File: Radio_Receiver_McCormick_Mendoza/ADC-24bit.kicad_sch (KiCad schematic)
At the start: 38 parts, among them J21 SDR Out, J22 Q_OUT, J30 Q_OUT, J31 Q_OUT, J32 Q_OUT, J41 V_DIV, J42 VDDA/2, J7 I_OUT, U10 OPA1612AxD, U12 PCM1808PWR

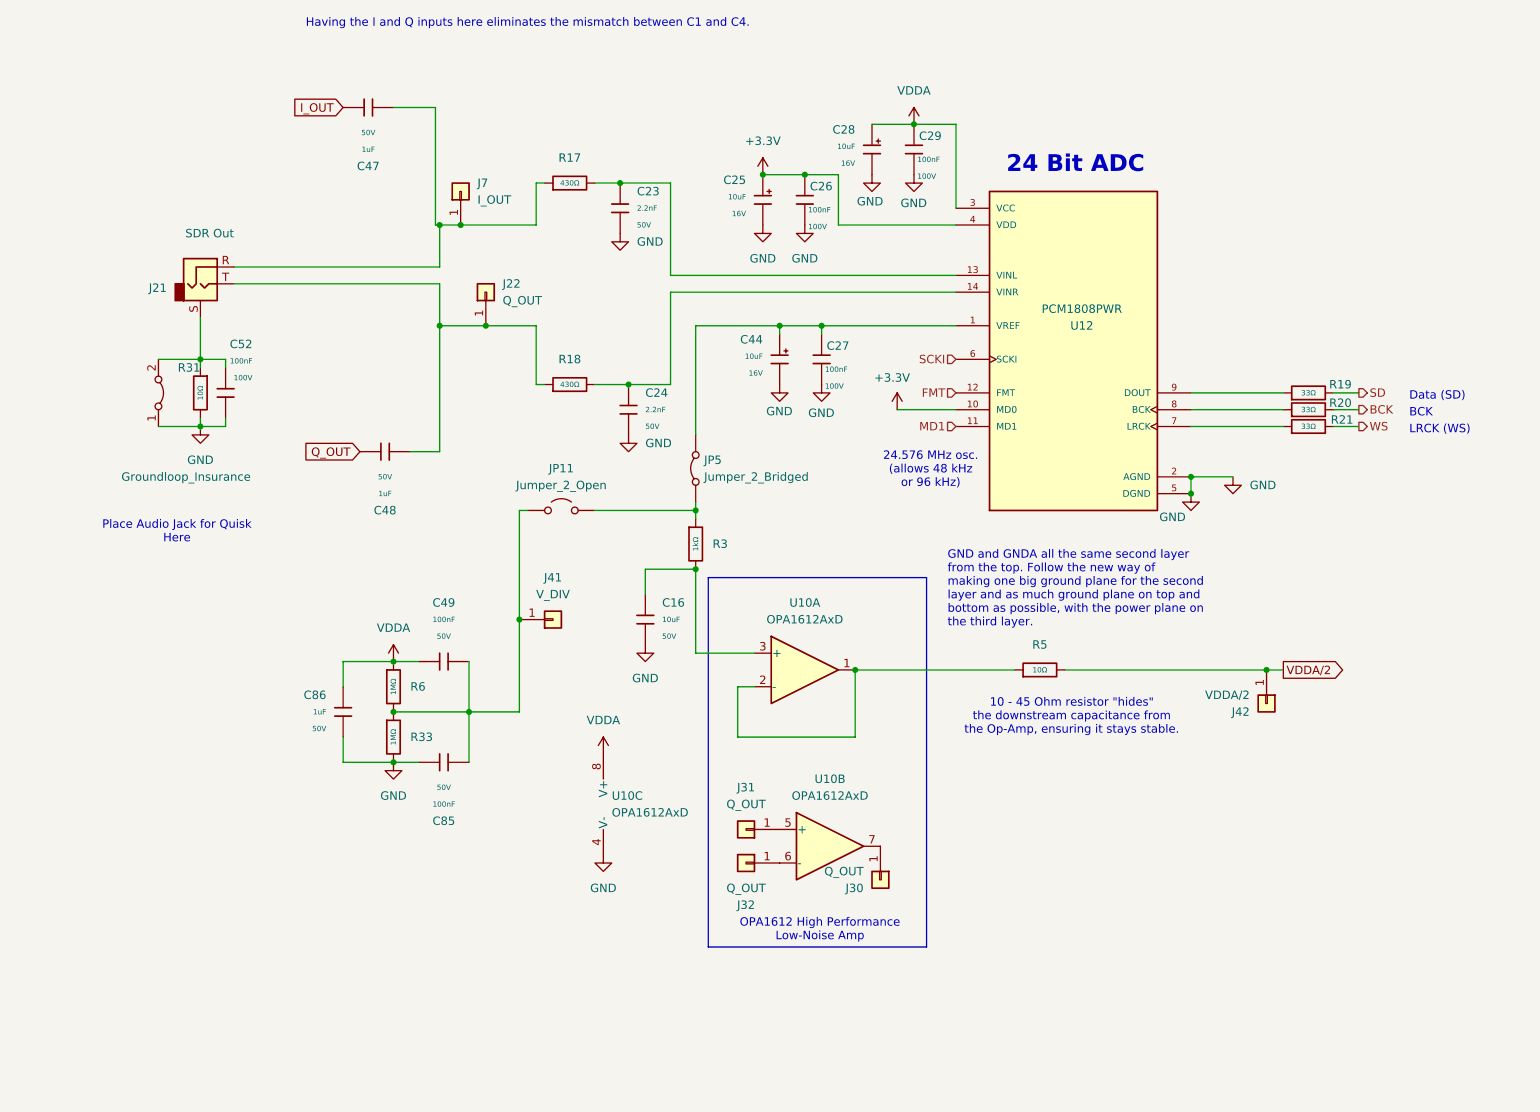
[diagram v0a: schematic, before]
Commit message: Finalized Pico connections and added indicator LEDs
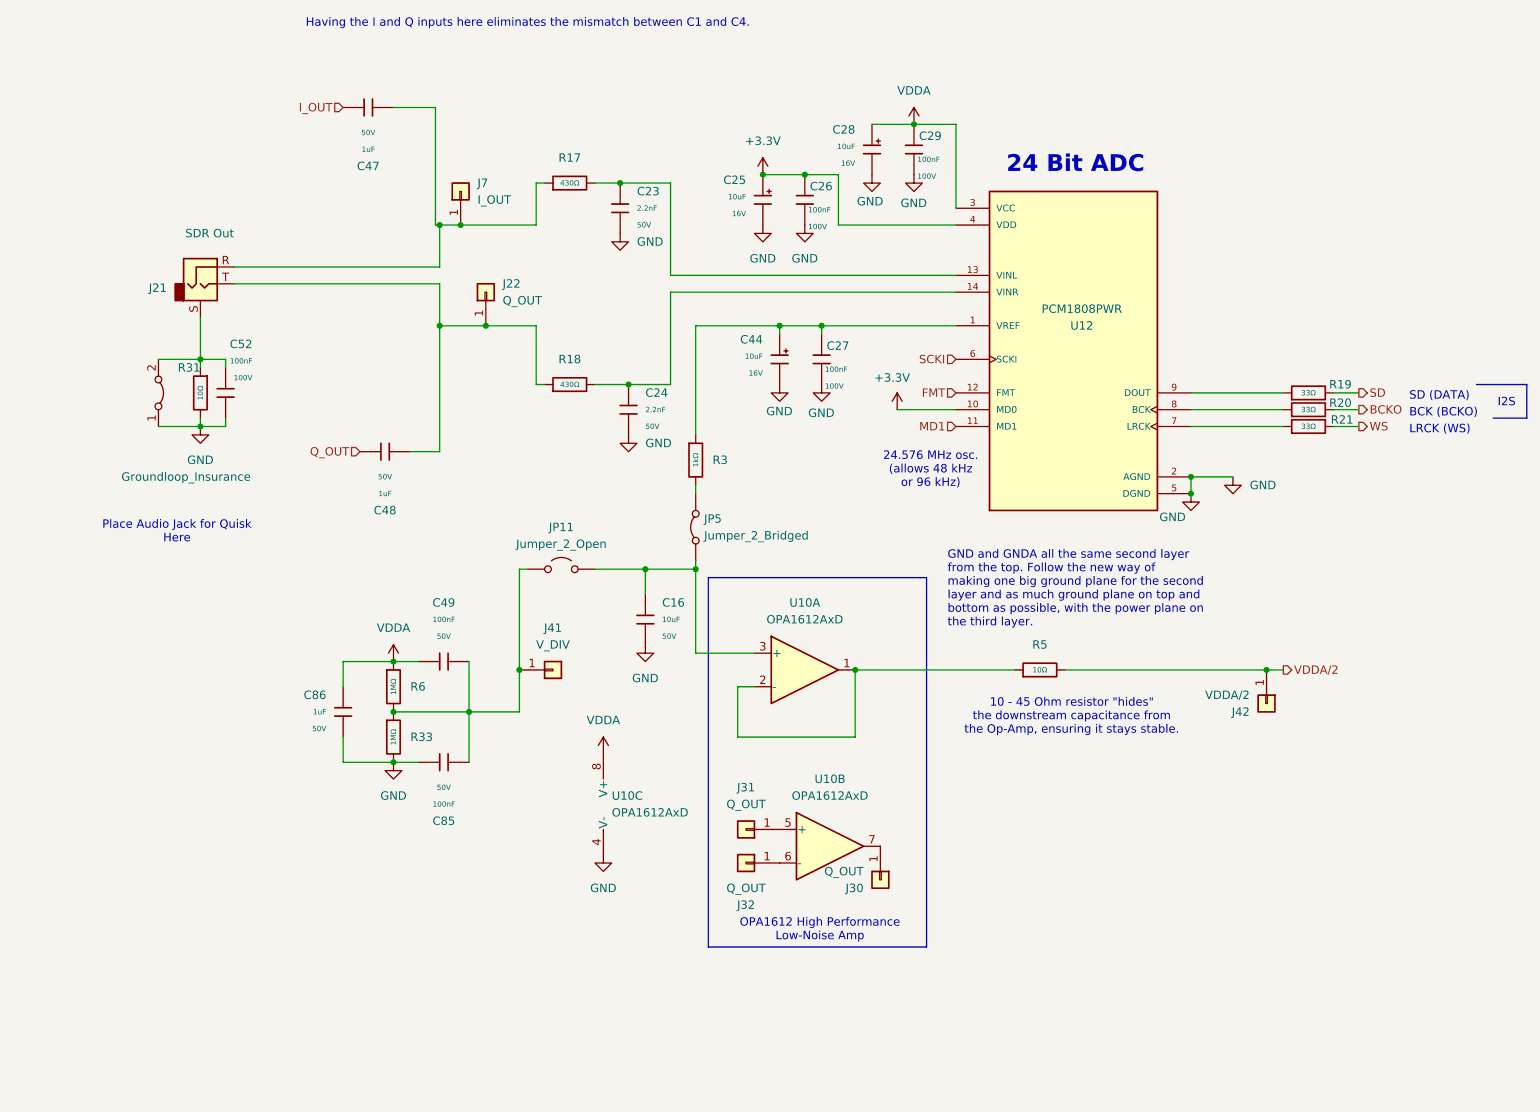
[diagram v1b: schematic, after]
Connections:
- net at JP11.2 (B), JP5.1 (A): now also C16.1, U10.3 (+); no longer R3.1
- net at C27.2, C44.1, U12.1 (VREF): now also R3.1; no longer JP5.2 (B)
- net BCK renamed BCKO
- new net: JP5.2 (B), R3.2
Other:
- note added: "BCK (BCKO)"
- note added: "I2S"
- note added: "SD (DATA)"
- note removed: "BCK"
- note removed: "Data (SD)"
- moved on the sheet: J41, JP11, JP5

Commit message: Added transformer footprint and datasheet
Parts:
- C47, C48, C49, C85, C86: Manufacturer Samsung Electro-Mechanics -> (none)
- R33, R6: Manufacturer UNI-ROYAL(Uniroyal Elec) -> (none)
- U10: footprint (none) -> OPA1612AID_SOIC8:D8-M; LCSC (none) -> C2871441; Price (none) -> 4.7846USD
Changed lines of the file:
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@@
 			)
 		)
-		(property "Manufacturer" "UNI-ROYAL(Uniroyal Elec)"
-			(at 81.28 125.73 0)
-			(hide yes)
-			(show_name no)
-			(do_not_autoplace no)
-			(effects
-				(font
-					(size 1.27 1.27)
-				)
-			)
-		)
 		(property "Part" "0603WAF1004T5E"
 			(at 81.28 125.73 0)
@@
 			)
 		)
-		(property "Manufacturer" "Samsung Electro-Mechanics"
-			(at 88.9 121.92 0)
-			(hide yes)
-			(show_name no)
-			(do_not_autoplace no)
-			(effects
-				(font
-					(size 1.27 1.27)
-				)
-			)
-		)
 		(property "Part" "CL05B104KB54PNC"
 			(at 88.9 121.92 0)
@@
 			)
 		)
-		(property "Manufacturer" "Samsung Electro-Mechanics"
-			(at 88.9 137.16 0)
-			(hide yes)
-			(show_name no)
-			(do_not_autoplace no)
-			(effects
-				(font
-					(size 1.27 1.27)
-				)
-			)
-		)
 		(property "Part" "CL05B104KB54PNC"
 			(at 88.9 137.16 0)
@@
 			)
 		)
-		(property "Manufacturer" "UNI-ROYAL(Uniroyal Elec)"
-			(at 81.28 133.35 0)
-			(hide yes)
-			(show_name no)
-			(do_not_autoplace no)
-			(effects
-				(font
-					(size 1.27 1.27)
-				)
-			)
-		)
 		(property "Part" "0603WAF1004T5E"
 			(at 81.28 133.35 0)
@@
 			)
 		)
-		(property "Footprint" ""
+		(property "Footprint" "OPA1612AID_SOIC8:D8-M"
 			(at 115.57 143.51 0)
 			(hide yes)
@@
 			)
 		)
+		(property "LCSC" "C2871441"
+			(at 115.57 143.51 0)
+			(hide yes)
+			(show_name no)
+			(do_not_autoplace no)
+			(effects
+				(font
+					(size 1.27 1.27)
+				)
+			)
+		)
+		(property "Price" "4.7846USD"
+			(at 115.57 143.51 0)
+			(hide yes)
+			(show_name no)
+			(do_not_autoplace no)
+			(effects
+				(font
+					(size 1.27 1.27)
+				)
+			)
+		)
 		(pin "4"
 		)
@@
 			)
 		)
-		(property "Manufacturer" "Samsung Electro-Mechanics"
-			(at 77.47 38.1 0)
-			(hide yes)
-			(show_name no)
-			(do_not_autoplace no)
-			(effects
-				(font
-					(size 1.27 1.27)
-				)
-			)
-		)
 		(property "Part" "CL21B105KBFNNNE"
 			(at 77.47 38.1 0)
@@
 			)
 		)
-		(property "Manufacturer" "Samsung Electro-Mechanics"
-			(at 80.01 90.17 0)
-			(hide yes)
-			(show_name no)
-			(do_not_autoplace no)
-			(effects
-				(font
-					(size 1.27 1.27)
-				)
-			)
-		)
 		(property "Part" "CL21B105KBFNNNE"
 			(at 80.01 90.17 0)
@@
 			)
 		)
-		(property "Footprint" ""
+		(property "Footprint" "OPA1612AID_SOIC8:D8-M"
 			(at 143.51 123.19 0)
 			(hide yes)
@@
 			)
 		)
+		(property "LCSC" "C2871441"
+			(at 143.51 123.19 0)
+			(hide yes)
+			(show_name no)
+			(do_not_autoplace no)
+			(effects
+				(font
+					(size 1.27 1.27)
+				)
+			)
+		)
+		(property "Price" "4.7846USD"
+			(at 143.51 123.19 0)
+			(hide yes)
+			(show_name no)
+			(do_not_autoplace no)
+			(effects
+				(font
+					(size 1.27 1.27)
+				)
+			)
+		)
 		(pin "4"
 		)
@@
 			)
 		)
-		(property "Manufacturer" "Samsung Electro-Mechanics"
-			(at 73.66 129.54 0)
-			(hide yes)
-			(show_name no)
-			(do_not_autoplace no)
-			(effects
-				(font
-					(size 1.27 1.27)
-				)
-			)
-		)
 		(property "Part" "CL10A105KB8NNNC"
 			(at 73.66 129.54 0)
@@
 			)
 		)
-		(property "Footprint" ""
+		(property "Footprint" "OPA1612AID_SOIC8:D8-M"
 			(at 147.32 149.86 0)
 			(hide yes)
@@
 			(at 147.32 149.86 0)
 			(hide yes)
+			(show_name no)
+			(do_not_autoplace no)
+			(effects
+				(font
+					(size 1.27 1.27)
+				)
+			)
+		)
+		(property "LCSC" "C2871441"
+			(at 147.32 149.86 0)
+			(hide yes)
+			(show_name no)
+			(do_not_autoplace no)
+			(effects
+				(font
+					(size 1.27 1.27)
+				)
+			)
+		)
+		(property "Price" "4.7846USD"
+			(at 147.32 149.86 0)
+			(hide yes)

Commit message: Swapped voltage regulator to output 4.5V
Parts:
- removed J22: Q_OUT, Connector_PinHeader_2.54mm:PinHeader_1x01_P2.54mm_Vertical, symbol Connector_Generic:Conn_01x01
- removed J7: I_OUT, Connector_PinHeader_2.54mm:PinHeader_1x01_P2.54mm_Vertical, symbol Connector_Generic:Conn_01x01
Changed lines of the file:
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@@
 	)
 	(junction
-		(at 91.44 55.88)
-		(diameter 0)
-		(color 0 0 0 0)
-	)
-	(junction
 		(at 146.05 71.12)
 		(diameter 0)
@@
 		(color 0 0 0 0)
 	)
-	(junction
-		(at 95.25 71.12)
-		(diameter 0)
-		(color 0 0 0 0)
-	)
 	(wire
 		(pts
@@
 	(wire
 		(pts
-			(xy 91.44 55.88) (xy 102.87 55.88)
+			(xy 88.265 55.88) (xy 102.87 55.88)
 		)
 		(stroke
@@
 	(wire
 		(pts
-			(xy 88.265 71.12) (xy 95.25 71.12)
-		)
-		(stroke
-			(width 0)
-			(type default)
-		)
-	)
-	(wire
-		(pts
 			(xy 123.19 63.5) (xy 166.37 63.5)
 		)
@@
 	(wire
 		(pts
-			(xy 95.25 71.12) (xy 102.87 71.12)
+			(xy 88.265 71.12) (xy 102.87 71.12)
 		)
 		(stroke
@@
 		)
 	)
-	(wire
-		(pts
-			(xy 88.265 55.88) (xy 91.44 55.88)
-		)
-		(stroke
-			(width 0)
-			(type default)
-		)
-	)
 	(hierarchical_label "Q_OUT"
 		(shape input)
@@
 	)
 	(symbol
-		(lib_id "Connector_Generic:Conn_01x01")
-		(at 95.25 66.04 90)
-		(unit 1)
-		(body_style 1)
-		(exclude_from_sim no)
-		(in_bom yes)
-		(on_board yes)
-		(in_pos_files yes)
-		(dnp no)
-		(fields_autoplaced yes)
-		(property "Reference" "J22"
-			(at 97.79 64.7699 90)
-			(show_name no)
-			(do_not_autoplace no)
-			(effects
-				(font
-					(size 1.27 1.27)
-				)
-				(justify right)
-			)
-		)
-		(property "Value" "Q_OUT"
-			(at 97.79 67.3099 90)
-			(show_name no)
-			(do_not_autoplace no)
-			(effects
-				(font
-					(size 1.27 1.27)
-				)
-				(justify right)
-			)
-		)
-		(property "Footprint" "Connector_PinHeader_2.54mm:PinHeader_1x01_P2.54mm_Vertical"
-			(at 95.25 66.04 0)
-			(hide yes)
-			(show_name no)
-			(do_not_autoplace no)
-			(effects
-				(font
-					(size 1.27 1.27)
-				)
-			)
-		)
-		(property "Datasheet" ""
-			(at 95.25 66.04 0)
-			(hide yes)
-			(show_name no)
-			(do_not_autoplace no)
-			(effects
-				(font
-					(size 1.27 1.27)
-				)
-			)
-		)
-		(property "Description" "Generic connector, single row, 01x01, script generated (kicad-library-utils/schlib/autogen/connector/)"
-			(at 95.25 66.04 0)
-			(hide yes)
-			(show_name no)
-			(do_not_autoplace no)
-			(effects
-				(font
-					(size 1.27 1.27)
-				)
-			)
-		)
-		(pin "1"
-		)
-		(instances
-			(project "Radio_Receiver_McCormick_Mendoza"
-				(path "/f31d31ab-6846-4f3a-92b1-aa5a6a13373f/f13b25c3-8e17-4875-84b2-896666dfe469"
-					(reference "J22")
-					(unit 1)
-				)
-			)
-		)
-	)
-	(symbol
 		(lib_name "Jumper_2_Bridged_1")
 		(lib_id "Jumper:Jumper_2_Bridged")
@@
 					(unit 1)
 				)
-			)
-		)
-	)
-	(symbol
-		(lib_id "Connector_Generic:Conn_01x01")
-		(at 91.44 50.8 90)
-		(unit 1)
-		(body_style 1)
-		(exclude_from_sim no)
-		(in_bom yes)
-		(on_board yes)
-		(in_pos_files yes)
-		(dnp no)
-		(fields_autoplaced yes)
-		(property "Reference" "J7"
-			(at 93.98 49.5299 90)
-			(show_name no)
-			(do_not_autoplace no)
-			(effects
-				(font
-					(size 1.27 1.27)
-				)
-				(justify right)
-			)
-		)
-		(property "Value" "I_OUT"
-			(at 93.98 52.0699 90)
-			(show_name no)
-			(do_not_autoplace no)
-			(effects
-				(font
-					(size 1.27 1.27)
-				)
-				(justify right)
-			)
-		)
-		(property "Footprint" "Connector_PinHeader_2.54mm:PinHeader_1x01_P2.54mm_Vertical"
-			(at 91.44 50.8 0)
-			(hide yes)
-			(show_name no)
-			(do_not_autoplace no)
-			(effects
-				(font
-					(size 1.27 1.27)
-				)
-			)
-		)
-		(property "Datasheet" ""
-			(at 91.44 50.8 0)
-			(hide yes)
-			(show_name no)
-			(do_not_autoplace no)
-			(effects
-				(font
-					(size 1.27 1.27)
-				)
-			)
-		)
-		(property "Description" "Generic connector, single row, 01x01, script generated (kicad-library-utils/schlib/autogen/connector/)"
-			(at 91.44 50.8 0)
-			(hide yes)
-			(show_name no)
-			(do_not_autoplace no)
-			(effects
-				(font
-					(size 1.27 1.27)
-				)
-			)
-		)
-		(pin "1"
-		)
-		(instances
-			(project "Radio_Receiver_McCormick_Mendoza"
-				(path "/f31d31ab-6846-4f3a-92b1-aa5a6a13373f/f13b25c3-8e17-4875-84b2-896666dfe469"
-					(reference "J7")
-					(unit 1)
-				)

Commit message: Corrected mono to headphones
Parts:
- U10: value OPA1612AxD -> OPA1612AID
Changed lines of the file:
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@@
 			)
 		)
-		(property "Value" "OPA1612AxD"
+		(property "Value" "OPA1612AID"
 			(at 114.3 144.7799 0)
 			(show_name no)
@@
 			)
 		)
-		(property "Value" "OPA1612AxD"
+		(property "Value" "OPA1612AID"
 			(at 143.51 115.57 0)
 			(show_name no)
@@
 			)
 		)
-		(property "Value" "OPA1612AxD"
+		(property "Value" "OPA1612AID"
 			(at 147.32 142.24 0)
 			(show_name no)
